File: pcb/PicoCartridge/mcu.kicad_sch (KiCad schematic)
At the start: 42 parts, among them J301 DBG, SW301 SW_Push, SW302 SW_Push, U1 RP2350B-QFN80, U2 W25Q128JVS, U3 MCP7940N-xSN, Y301 Crystal_GND24, Y302 Crystal

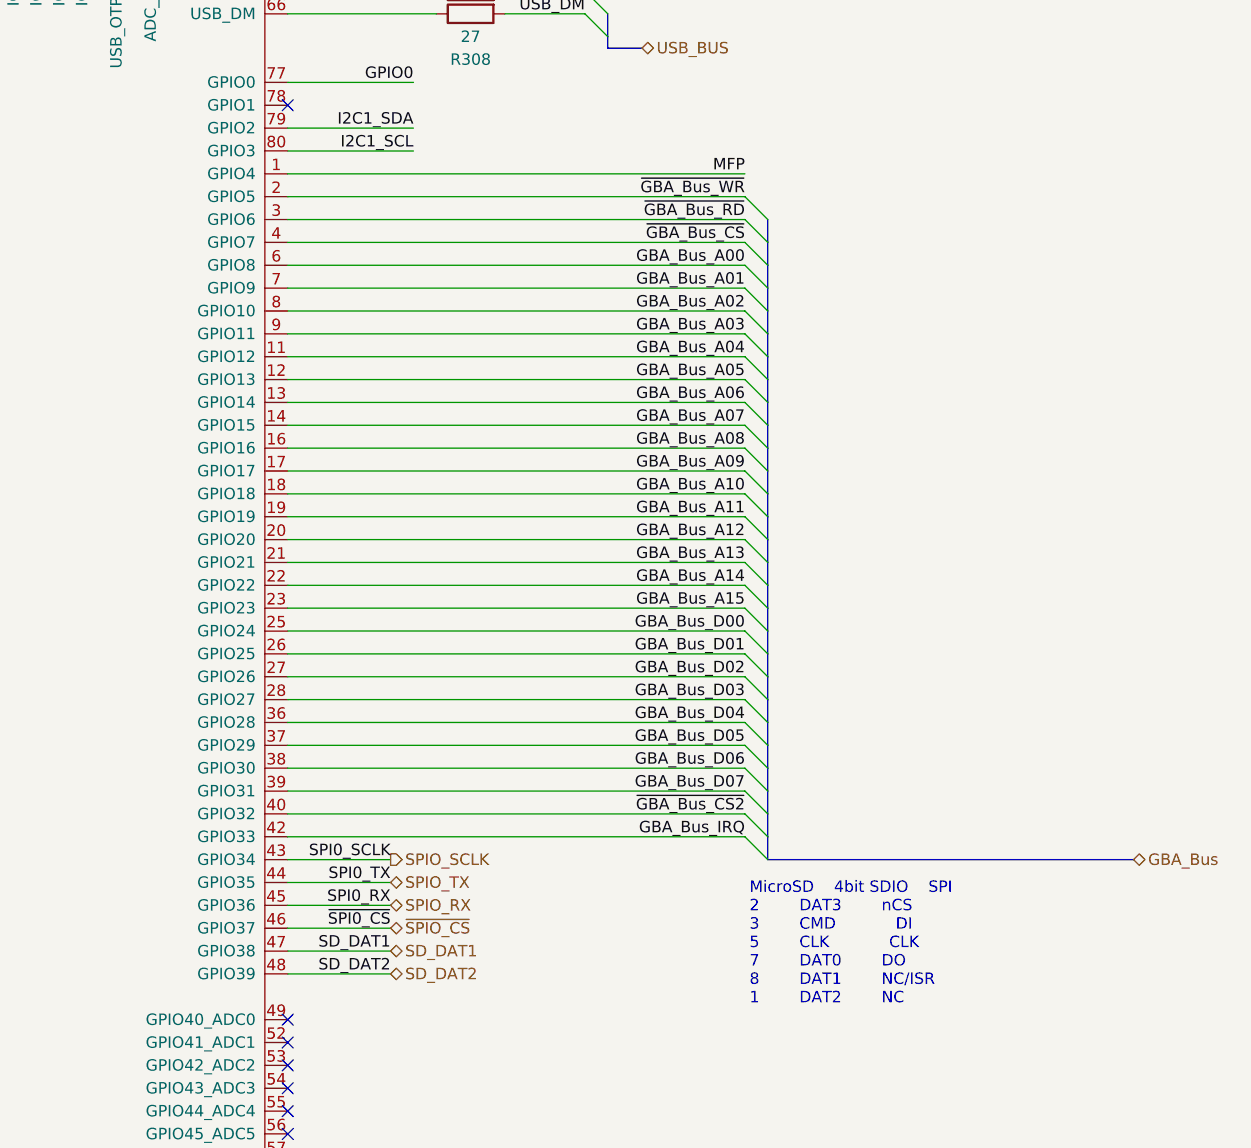
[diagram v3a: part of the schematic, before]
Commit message: Fixed GBA bus internal logic
THe GBA bus is now a correct bus in a sense of kicad
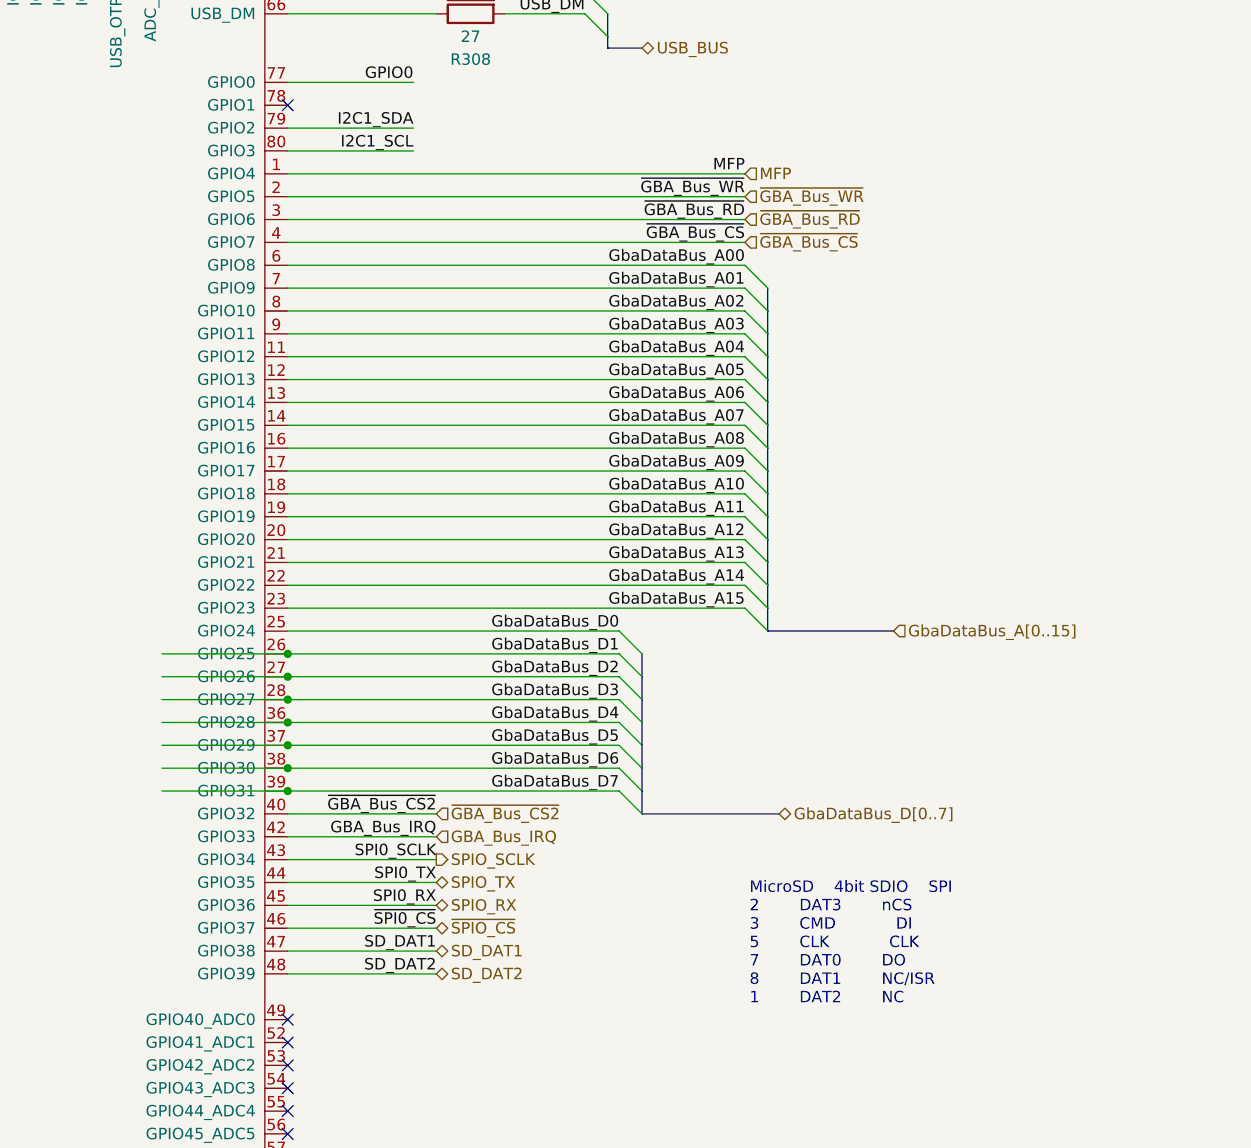
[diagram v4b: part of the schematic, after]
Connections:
- net GBA_Bus_A00 renamed GbaDataBus_A00
- net GBA_Bus_A01 renamed GbaDataBus_A01
- net GBA_Bus_A02 renamed GbaDataBus_A02
- net GBA_Bus_A03 renamed GbaDataBus_A03
- net GBA_Bus_A04 renamed GbaDataBus_A04
- net GBA_Bus_A05 renamed GbaDataBus_A05
- net GBA_Bus_A06 renamed GbaDataBus_A06
- net GBA_Bus_A07 renamed GbaDataBus_A07
- net GBA_Bus_A08 renamed GbaDataBus_A08
- net GBA_Bus_A09 renamed GbaDataBus_A09
- net GBA_Bus_A10 renamed GbaDataBus_A10
- net GBA_Bus_A11 renamed GbaDataBus_A11
- net GBA_Bus_A12 renamed GbaDataBus_A12
- net GBA_Bus_A13 renamed GbaDataBus_A13
- net GBA_Bus_A14 renamed GbaDataBus_A14
- net GBA_Bus_A15 renamed GbaDataBus_A15
- net GBA_Bus_D00 renamed GbaDataBus_D0
- net GBA_Bus_D01 renamed GbaDataBus_D1
- net GBA_Bus_D02 renamed GbaDataBus_D2
- net GBA_Bus_D03 renamed GbaDataBus_D3
- net GBA_Bus_D04 renamed GbaDataBus_D4
- net GBA_Bus_D05 renamed GbaDataBus_D5
- net GBA_Bus_D06 renamed GbaDataBus_D6
- net GBA_Bus_D07 renamed GbaDataBus_D7

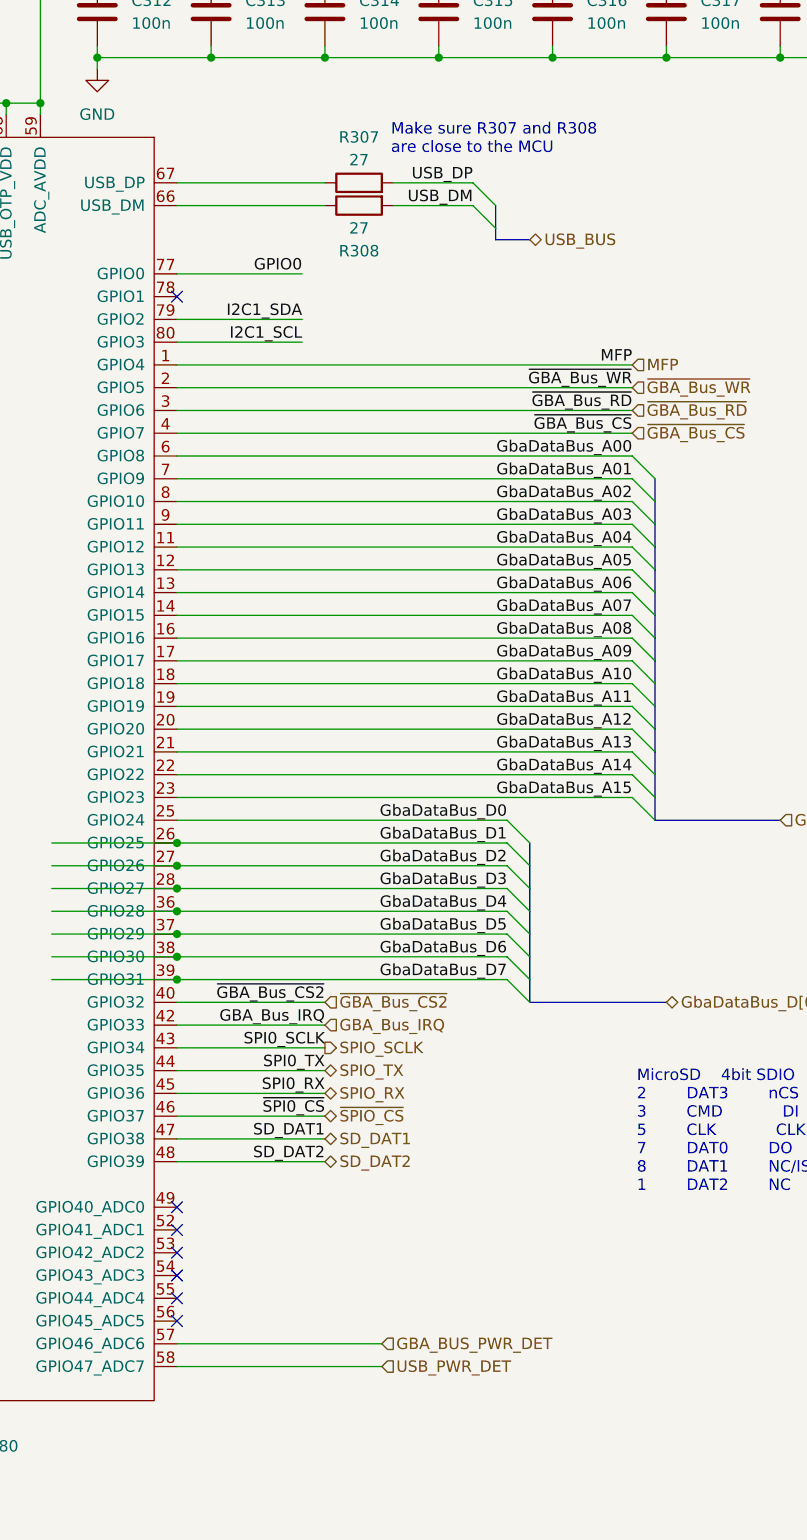
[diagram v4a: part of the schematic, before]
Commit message: Removed dedicated usb connector
Use would be very limited (live view on a pc and data transfer without
removing the sd card) and increases the pcb & schematic complexity by a lot.

Removing the usb connector for this revision. It is possible, if this design
is successful that I will create a new revision at some point. You never know.
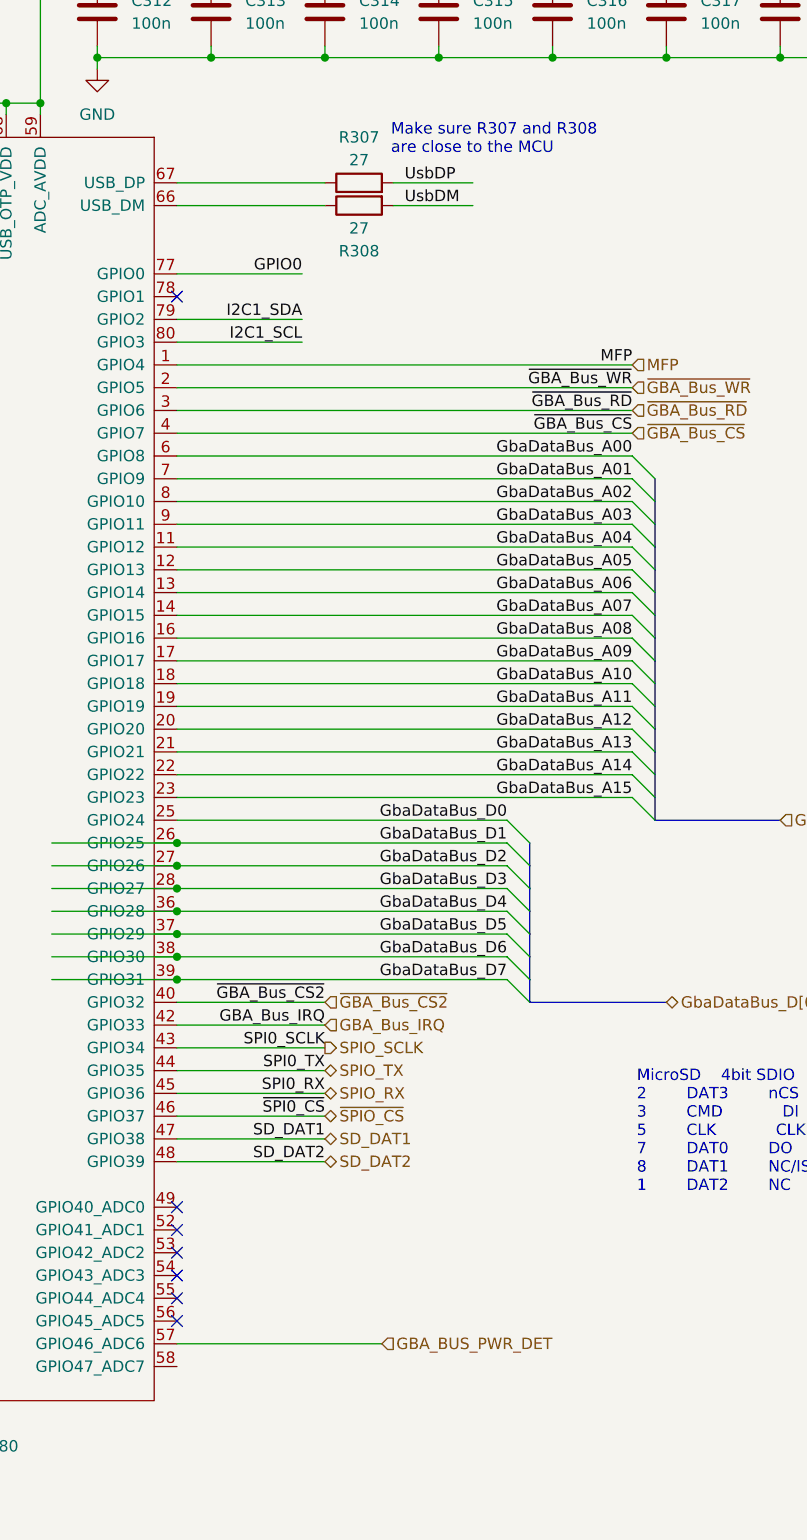
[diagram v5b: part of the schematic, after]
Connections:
- net USB_DM renamed UsbDM
- net USB_DP renamed UsbDP
- net USB_PWR_DET: no longer names the net of U1.58 (GPIO47_ADC7)
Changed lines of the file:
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@@
 	)
 	(bus_entry
-		(at 276.86 78.74)
-		(size 2.54 2.54)
-		(stroke
-			(width 0)
-			(type default)
-		)
-	)
-	(bus_entry
 		(at 294.64 137.16)
 		(size 2.54 2.54)
@@
 	)
 	(bus_entry
-		(at 276.86 76.2)
-		(size 2.54 2.54)
-		(stroke
-			(width 0)
-			(type default)
-		)
-	)
-	(bus_entry
 		(at 294.64 114.3)
 		(size 2.54 2.54)
@@
 	(wire
 		(pts
-			(xy 243.84 208.28) (xy 266.7 208.28)
-		)
-		(stroke
-			(width 0)
-			(type default)
-		)
-	)
-	(wire
-		(pts
 			(xy 173.99 121.92) (xy 162.56 121.92)
 		)
@@
 		)
 	)
-	(bus
-		(pts
-			(xy 283.21 82.55) (xy 279.4 82.55)
-		)
-		(stroke
-			(width 0)
-			(type default)
-		)
-	)
 	(wire
 		(pts
@@
 		)
 	)
-	(bus
-		(pts
-			(xy 279.4 78.74) (xy 279.4 81.28)
-		)
-		(stroke
-			(width 0)
-			(type default)
-		)
-	)
 	(wire
 		(pts
@@
 		)
 	)
-	(bus
-		(pts
-			(xy 279.4 81.28) (xy 279.4 82.55)
-		)
-		(stroke
-			(width 0)
-			(type default)
-		)
-	)
 	(wire
 		(pts
@@
 		)
 	)
-	(label "USB_DM"
-		(at 276.86 78.74 180)
-		(fields_autoplaced yes)
-		(effects
-			(font
-				(size 1.27 1.27)
-			)
-			(justify right bottom)
-		)
-	)
 	(label "GbaDataBus_A11"
 		(at 294.64 134.62 180)
@@
 		)
 	)
+	(label "UsbDM"
+		(at 269.24 78.74 0)
+		(fields_autoplaced yes)
+		(effects
+			(font
+				(size 1.27 1.27)
+			)
+			(justify left bottom)
+		)
+	)
 	(label "I2C1_SDA"
 		(at 78.74 224.79 180)
@@
 		)
 	)
-	(label "USB_DP"
-		(at 276.86 76.2 180)
-		(fields_autoplaced yes)
-		(effects
-			(font
-				(size 1.27 1.27)
-			)
-			(justify right bottom)
-		)
-	)
 	(label "SPI0_RX"
 		(at 260.35 177.8 180)
@@
 		)
 	)
+	(label "UsbDP"
+		(at 269.24 76.2 0)
+		(fields_autoplaced yes)
+		(effects
+			(font
+				(size 1.27 1.27)
+			)
+			(justify left bottom)
+		)
+	)
 	(label "XOUT"
 		(at 162.56 127 0)
@@
 		)
 	)
-	(hierarchical_label "USB_PWR_DET"
-		(shape input)
-		(at 266.7 208.28 0)
-		(fields_autoplaced yes)
-		(effects
-			(font
-				(size 1.27 1.27)
-			)
-			(justify left)
-		)
-	)
 	(hierarchical_label "GBA_BUS_PWR_DET"
 		(shape input)
@@
 		(fields_autoplaced yes)
 		(effects
-			(font
-				(size 1.27 1.27)
-			)
-			(justify left)
-		)
-	)
-	(hierarchical_label "USB_BUS"
-		(shape bidirectional)
-		(at 283.21 82.55 0)
-		(fields_autoplaced yes)
-		(effects

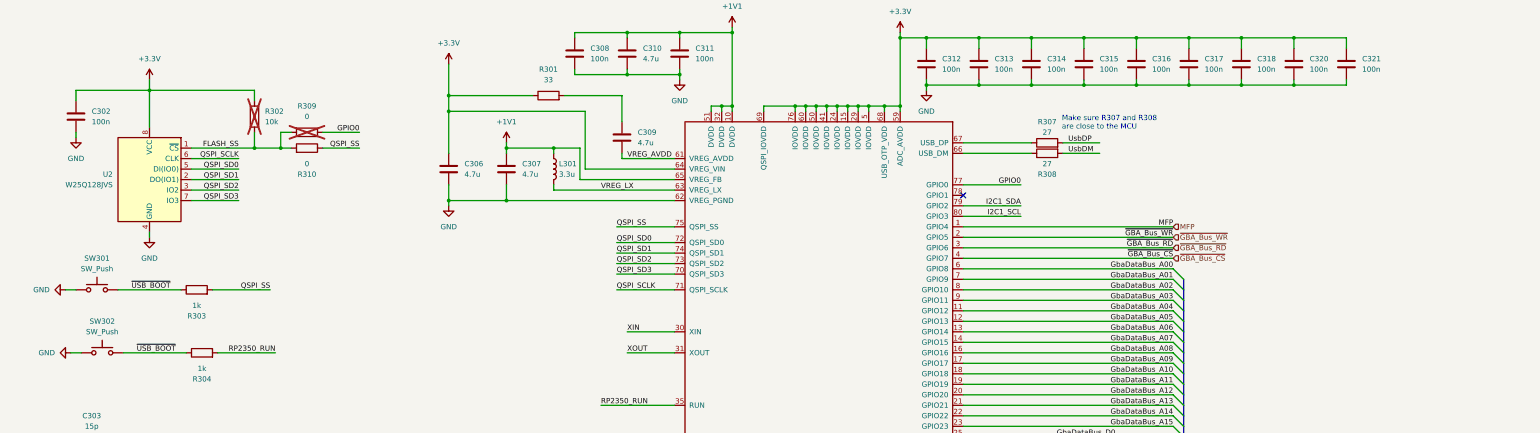
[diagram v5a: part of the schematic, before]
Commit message: Added programmer "connector"
Additionally removed reset and program switches as there is no need for
them on the pcb itself if there is no usb connection.
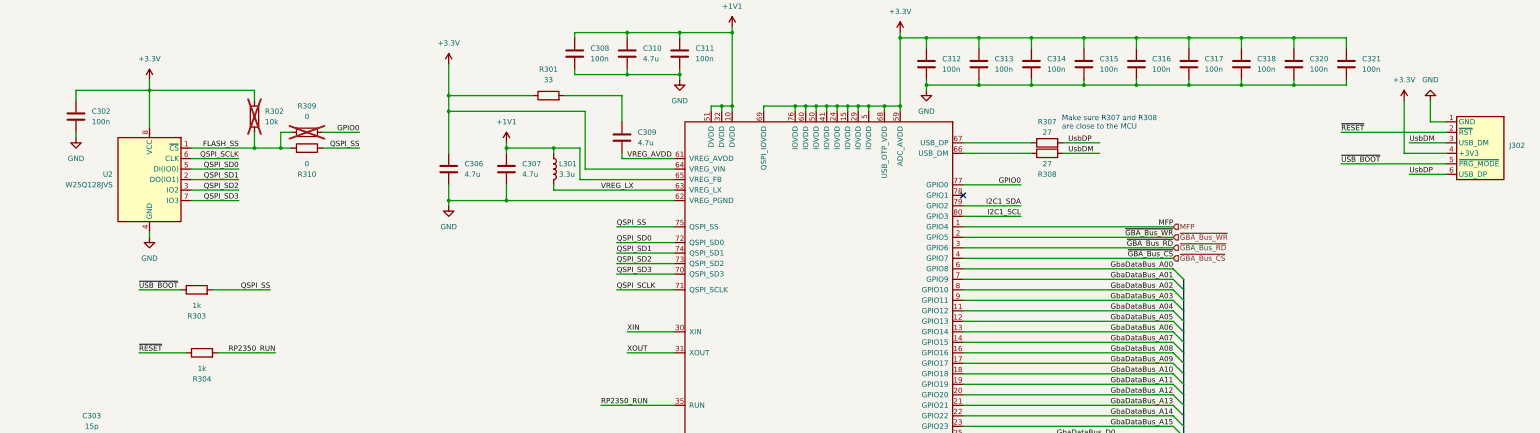
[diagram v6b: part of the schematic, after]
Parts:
- removed SW301, SW302: SW_Push, symbol Switch:SW_Push
- added J302: ~, PicoCartridge:ProgrammerConnector_SMD, symbol PicoCartridge:Programmer
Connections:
- net +3.3V: now also J302.4 (+3V3)
- net GND: now also J302.1 (GND)
- net UsbDM: now also J302.3 (USB_DM)
- net UsbDP: now also J302.6 (USB_DP)
- net ~{USB_BOOT}: now also J302.5 (~{PRG_MODE}); no longer R304.1
- new net ~{RESET}: J302.2 (~{RST}), R304.1

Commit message: Upload progress
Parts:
- Y302: footprint (none) -> Crystal:Crystal_DS26_D2.0mm_L6.0mm_Horizontal; LCSC# (none) -> C2681251
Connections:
- net at C323.2, U3.2 (X2): now also Y302.2; no longer Y302.1
- net at C322.2, U3.1 (X1): now also Y302.1; no longer Y302.2
- net GbaDataBus_A00 renamed GbaDataBus_A0
- net GbaDataBus_A01 renamed GbaDataBus_A1
- net GbaDataBus_A02 renamed GbaDataBus_A2
- net GbaDataBus_A03 renamed GbaDataBus_A3
- net GbaDataBus_A04 renamed GbaDataBus_A4
- net GbaDataBus_A05 renamed GbaDataBus_A5
- net GbaDataBus_A06 renamed GbaDataBus_A6
- net GbaDataBus_A07 renamed GbaDataBus_A7
- net GbaDataBus_A08 renamed GbaDataBus_A8
- net GbaDataBus_A09 renamed GbaDataBus_A9
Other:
- moved on the sheet: Y302
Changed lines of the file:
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@@
 		)
 	)
-	(label "GbaDataBus_A00"
+	(label "GbaDataBus_A0"
 		(at 294.64 106.68 180)
 		(fields_autoplaced yes)
@@
 		)
 	)
-	(label "GbaDataBus_A01"
+	(label "GbaDataBus_A1"
 		(at 294.64 109.22 180)
 		(fields_autoplaced yes)
@@
 		)
 	)
-	(label "GbaDataBus_A07"
+	(label "GbaDataBus_A7"
 		(at 294.64 124.46 180)
 		(fields_autoplaced yes)
@@
 		)
 	)
-	(label "GbaDataBus_A02"
+	(label "GbaDataBus_A2"
 		(at 294.64 111.76 180)
 		(fields_autoplaced yes)
@@
 		)
 	)
-	(label "GbaDataBus_A05"
+	(label "GbaDataBus_A5"
 		(at 294.64 119.38 180)
 		(fields_autoplaced yes)
@@
 		)
 	)
-	(label "GbaDataBus_A09"
+	(label "GbaDataBus_A9"
 		(at 294.64 129.54 180)
 		(fields_autoplaced yes)
@@
 		)
 	)
-	(label "GbaDataBus_A08"
+	(label "GbaDataBus_A8"
 		(at 294.64 127 180)
 		(fields_autoplaced yes)
@@
 		)
 	)
-	(label "GbaDataBus_A04"
+	(label "GbaDataBus_A4"
 		(at 294.64 116.84 180)
 		(fields_autoplaced yes)
@@
 		)
 	)
-	(label "GbaDataBus_A06"
+	(label "GbaDataBus_A6"
 		(at 294.64 121.92 180)
 		(fields_autoplaced yes)
@@
 		)
 	)
-	(label "GbaDataBus_A03"
+	(label "GbaDataBus_A3"
 		(at 294.64 114.3 180)
 		(fields_autoplaced yes)
@@
 	(symbol
 		(lib_id "Device:Crystal")
-		(at 34.29 227.33 90)
+		(at 34.29 227.33 270)
 		(unit 1)
 		(exclude_from_sim no)
@@
 					(size 1.27 1.27)
 				)
-				(justify right)
+				(justify left)
 			)
 		)
@@
 					(size 1.27 1.27)
 				)
-				(justify right)
-			)
-		)
-		(property "Footprint" ""
+				(justify left)
+			)
+		)
+		(property "Footprint" "Crystal:Crystal_DS26_D2.0mm_L6.0mm_Horizontal"
 			(at 34.29 227.33 0)
 			(effects
@@
 			)
 		)
-		(property "Datasheet" "~"
+		(property "Datasheet" "https://www.lcsc.com/datasheet/lcsc_datasheet_2106070533_JYJE-Q2632768BWNAC_C2681251.pdf"
 			(at 34.29 227.33 0)
 			(effects
@@
 			(effects
 				(font
+					(size 1.27 1.27)
+				)
+				(hide yes)
+			)
+		)
+		(property "LCSC#" "C2681251"
+			(at 34.29 227.33 90)
+			(effects
+				(font
